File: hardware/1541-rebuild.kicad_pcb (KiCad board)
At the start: 2 copper layers, 76.2 x 97.8 mm, 30 parts, among them CON1 SD_Card, IC1 ATMEGA1284P-P, J1 ISP, J2 KEYS, J3 EXT_5V, J4 RESET CONN, J5 PC7, J6 LCD Display, P1 VIA_PIN_1-20, P2 VIA-6522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

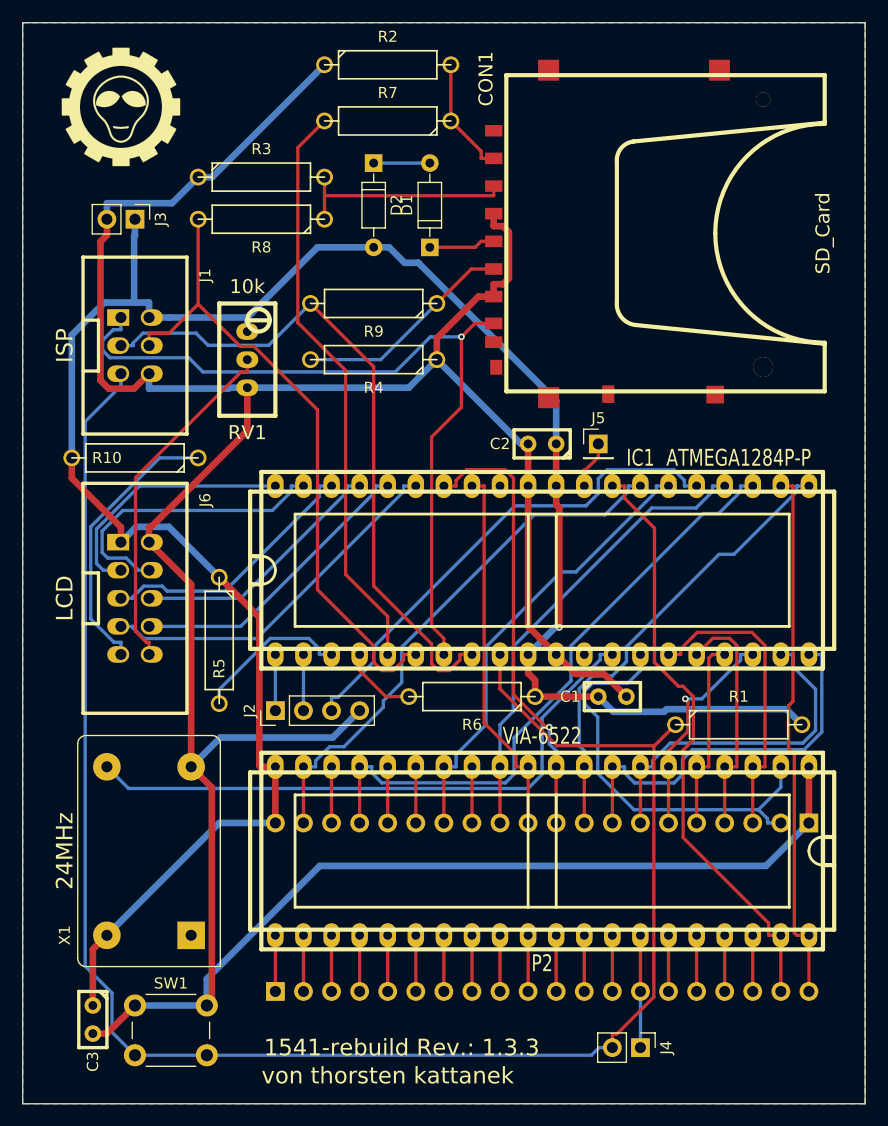
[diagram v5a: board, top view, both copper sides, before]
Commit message: - Hardware nochmal angepasst - erstes Layout erstellt - Schaltplan auf Rev.1.3.4 gesetzt
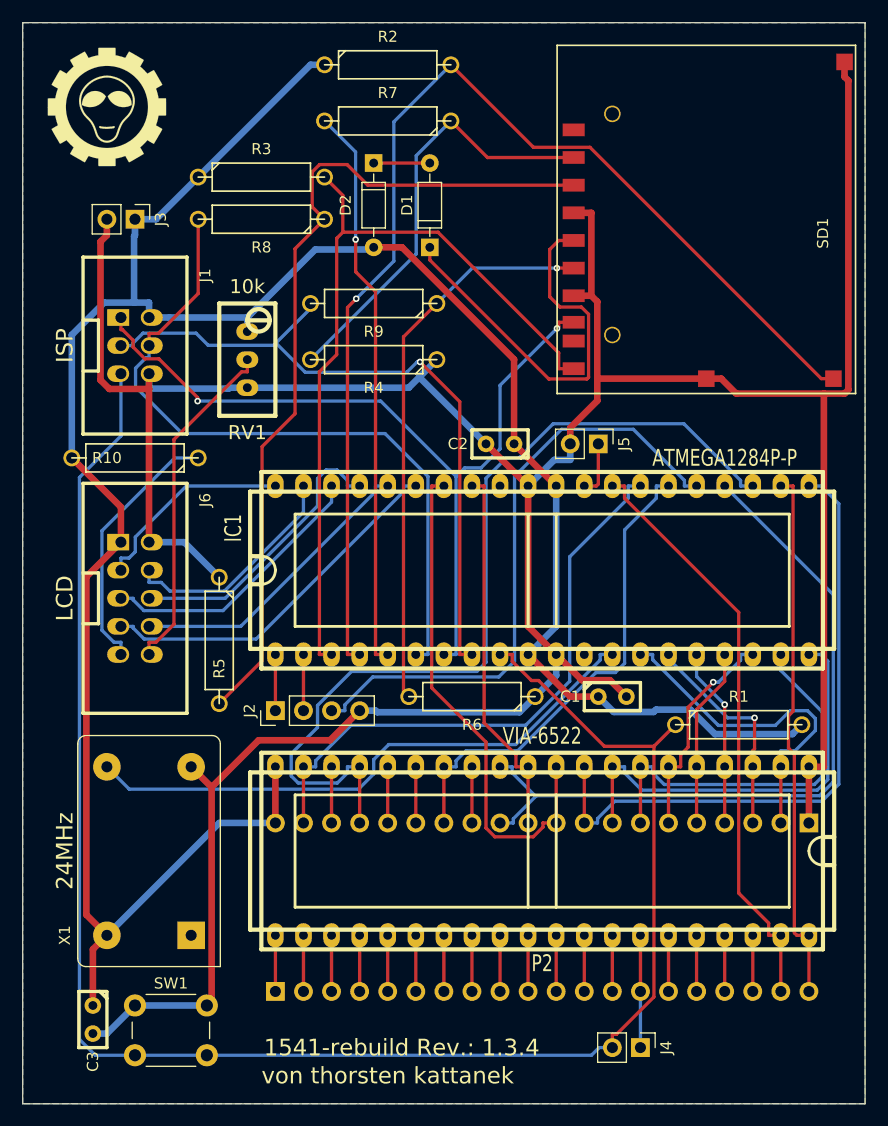
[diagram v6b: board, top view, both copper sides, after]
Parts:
- removed CON1: SD_Card, w_conn_misc:sd_socket
- removed the G*** at (116.8, 49.5)
- added G***: LOGO, ka_logos:logo_01_10_7mm_fsilk, F.Cu at (115.6, 49.5)
- added SD1: SD_Socket, ka_sd_sockets:SD_Socket_104D-TCA0-R06, F.Cu at (161.3, 61.0)
- J5: footprint Pin_Headers:Pin_Header_Straight_1x01_Pitch2.54mm -> Pin_Headers:Pin_Header_Straight_1x02_Pitch2.54mm
- R2: value 3,3k -> 47k
- R3: value 3,3k -> 47kR
- R5: value 47k -> 3,3k
- R6: value 47kR -> 3,3k
- moved C2 3.81 mm to (151.1, 80.0)
- turned J5 to 270 degrees
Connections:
- R2 pad 1: GND -> +5V
- R2 pad 2: Net-(CON1-Pad1) -> /SD Karte/SD_WP
- R3 pad 1: GND -> +5V
- R3 pad 2: Net-(CON1-Pad2) -> /SD Karte/SD_DETECT
- R4 pad 2: Net-(CON1-Pad5) -> Net-(R4-Pad2)
- R5 pad 1: +5V -> GND
- R5 pad 2: /SD Karte/SD_DETECT -> Net-(R5-Pad2)
- R6 pad 1: +5V -> GND
- R6 pad 2: /SD Karte/SD_WP -> Net-(R6-Pad2)
- R7 pad 1: Net-(CON1-Pad1) -> Net-(R4-Pad2)
- R8 pad 1: Net-(CON1-Pad2) -> Net-(R5-Pad2)
- R9 pad 1: Net-(CON1-Pad5) -> Net-(R6-Pad2)
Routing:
- net /SD Karte/SD_WP: track 6.87 -> 104.7 mm, vias 0 -> 1
- net Net-(R5-Pad2): track 0.00 -> 77.2 mm
- net /SD Karte/SD_DETECT: track 14.2 -> 72.7 mm
- net Net-(R6-Pad2): track 0.00 -> 50.7 mm, vias 0 -> 1
- net Net-(R4-Pad2): track 0.00 -> 39.3 mm
- net Net-(D1-Pad1): track 6.00 -> 36.7 mm
- net +5V: track 200.9 -> 228.4 mm, vias 1 -> 0
- net /VIA 6522 Sockel/MTR: track 41.9 -> 67.4 mm
- net /VIA 6522 Sockel/SYNC: track 56.8 -> 82.1 mm
- net Net-(CON1-Pad2): track 20.0 -> 0.00 mm
- net Net-(CON1-Pad5): track 20.0 -> 0.00 mm
- net /VIA 6522 Sockel/PA7: track 41.8 -> 58.5 mm
- net GND: track 291.3 -> 305.3 mm
- net Net-(IC1-Pad25): track 45.2 -> 56.1 mm
- net Net-(CON1-Pad1): track 10.7 -> 0.00 mm
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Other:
- board text added: "1541-rebuild Rev.: 1.3.4"
- board text removed: "1541-rebuild Rev.: 1.3.3"

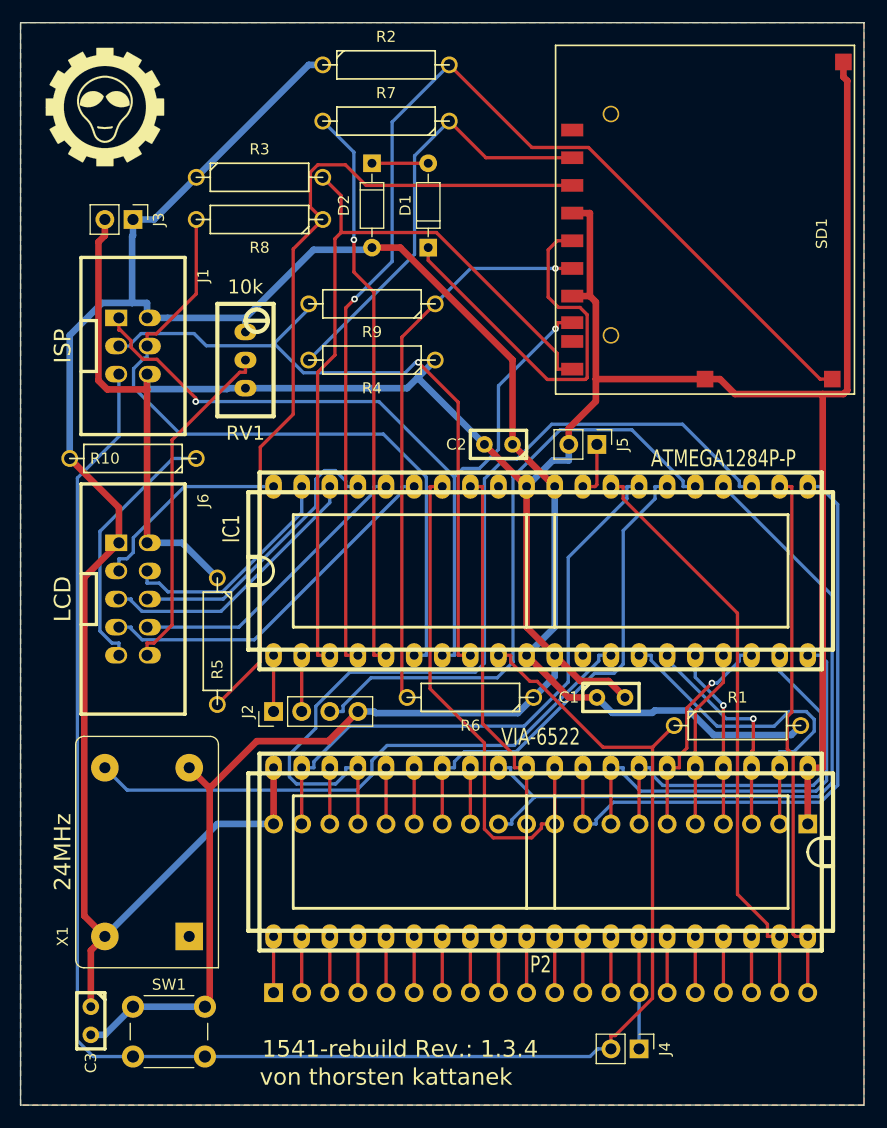
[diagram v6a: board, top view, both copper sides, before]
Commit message: Borad fertig gestellt und auf rev 1.3.5 gesetzt Gerberfiles erzeugt und als rar gepackt. Mit PCB Hersteller -Seedstudio- getestet.
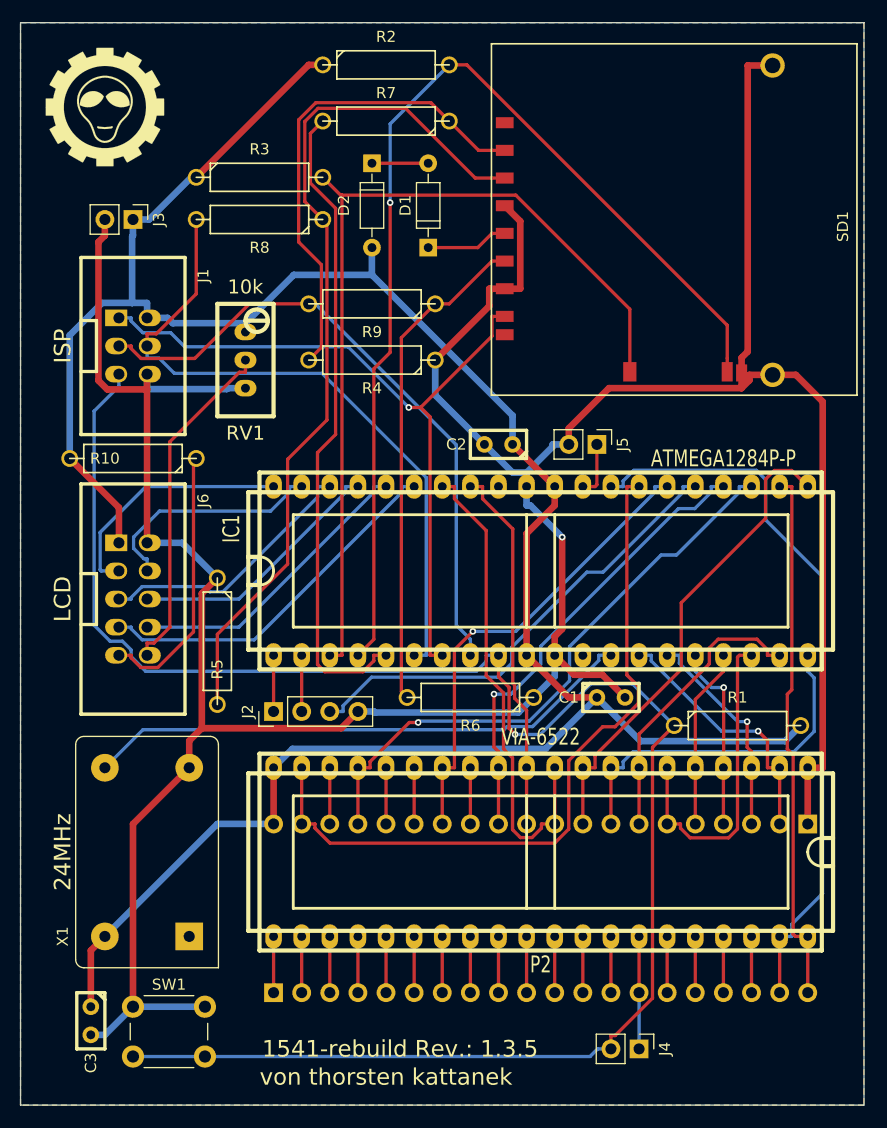
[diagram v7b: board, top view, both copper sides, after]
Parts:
- SD1: value SD_Socket -> ATTEND_104H-TDA0-R01; footprint ka_sd_sockets:SD_Socket_104D-TCA0-R06 -> ka_sd_sockets:ATTEND_104H-TDA0-R01
- moved SD1 14.6 mm to (175.9, 60.3)
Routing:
- net Net-(D1-Pad1): track 36.7 -> 7.45 mm
- net /VIA 6522 Sockel/SYNC: track 82.1 -> 53.6 mm, vias 0 -> 1
- net /VIA 6522 Sockel/MTR: track 67.4 -> 41.6 mm, vias 0 -> 1
- net /VIA 6522 Sockel/PA7: track 58.5 -> 43.4 mm
- net Net-(IC1-Pad25): track 56.1 -> 42.9 mm
- net /VIA 6522 Sockel/OE: track 53.6 -> 66.4 mm
- net /VIA 6522 Sockel/SOE: track 53.3 -> 66.0 mm
- net /VIA 6522 Sockel/PA4: track 20.0 -> 29.4 mm, vias 1 -> 0
- net /VIA 6522 Sockel/PA5: track 35.4 -> 26.1 mm
- net /SD Karte/SD_WP: track 104.7 -> 95.8 mm
- net /SD Karte/SD_DETECT: track 72.7 -> 81.0 mm
- net +5V: track 228.4 -> 220.3 mm
- net /SD Karte/MISO: track 74.7 -> 66.7 mm, vias 2 -> 1
- net /VIA 6522 Sockel/PA0: track 31.1 -> 23.7 mm, vias 0 -> 1
- net /SD Karte/SS: track 51.3 -> 58.5 mm, vias 1 -> 0
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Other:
- board text added: "1541-rebuild Rev.: 1.3.5"
- board text removed: "1541-rebuild Rev.: 1.3.4"

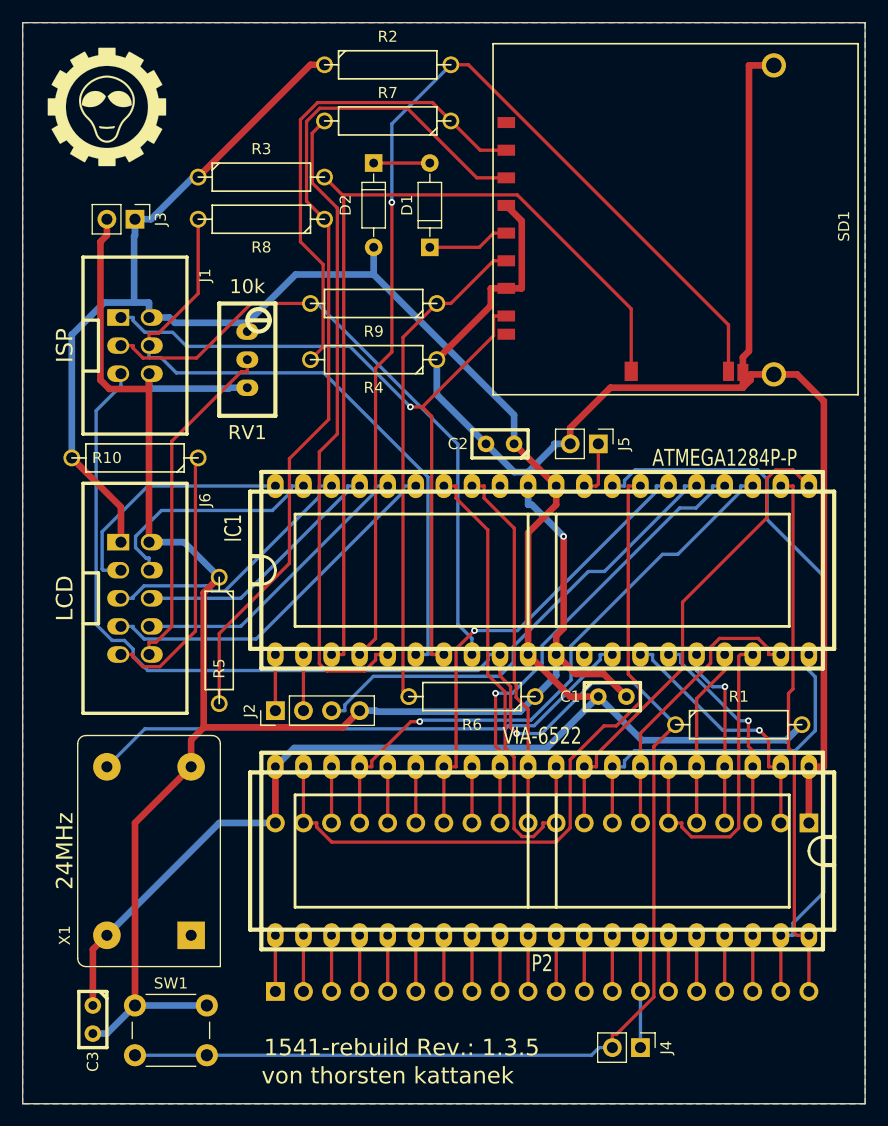
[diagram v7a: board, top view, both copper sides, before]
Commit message: Hardware Projekt knovertiert von KiCad 4 -> KiCad 5 - Schaltplan angepasst - neues Detailfoto hinzugefügt - Footprints neu zugeordnet, somit ist auch wieder eine 3D Darstellung möglich - Readme.md angepasst
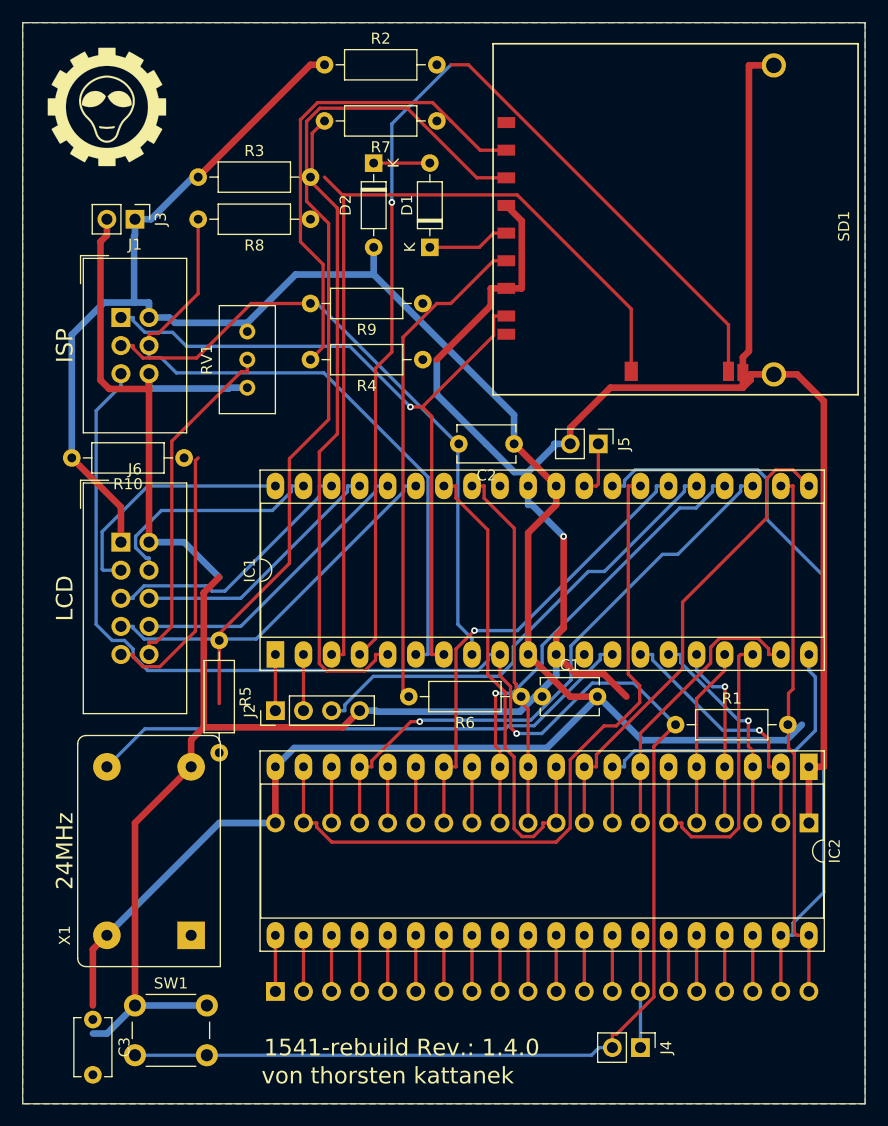
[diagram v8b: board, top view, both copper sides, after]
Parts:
- removed the G*** at (115.6, 49.5)
- removed P3: VIA_PIN_21-40, Pin_Headers:Pin_Header_Straight_1x20_Pitch2.54mm
- added G***: LOGO, logos_tk:logo_01_10_7mm_fsilk, F.Cu at (115.6, 49.5)
- added IC2: VIA6522, Package_DIP:DIP-40_W15.24mm_Socket_LongPads, F.Cu at (179.1, 109.2)
- C1, C2, C3: footprint w_capacitors:cnp_3mm_disc -> Capacitor_THT:C_Disc_D5.1mm_W3.2mm_P5.00mm
- D1, D2: footprint Diodes_THT:D_DO-35_SOD27_P7.62mm_Horizontal -> Diode_THT:D_DO-35_SOD27_P7.62mm_Horizontal
- IC1: footprint w_pth_circuits:dil_40-600_socket -> Package_DIP:DIP-40_W15.24mm_Socket_LongPads
- J1: footprint w_conn_strip:vasch_strip_3x2 -> Connector_IDC:IDC-Header_2x03_P2.54mm_Vertical
- J2: footprint Pin_Headers:Pin_Header_Straight_1x04_Pitch2.54mm -> Connector_PinHeader_2.54mm:PinHeader_1x04_P2.54mm_Vertical
- J3, J4, J5: footprint Pin_Headers:Pin_Header_Straight_1x02_Pitch2.54mm -> Connector_PinHeader_2.54mm:PinHeader_1x02_P2.54mm_Vertical
- J6: footprint w_conn_strip:vasch_strip_5x2 -> Connector_IDC:IDC-Header_2x05_P2.54mm_Vertical
- P1: footprint Pin_Headers:Pin_Header_Straight_1x20_Pitch2.54mm -> Connector_PinHeader_2.54mm:PinHeader_1x20_P2.54mm_Vertical
- P2: value VIA-6522 -> VIA_PIN_21-40; footprint w_pth_circuits:dil_40-600_socket -> Connector_PinHeader_2.54mm:PinHeader_1x20_P2.54mm_Vertical; moved to B.Cu
- R1, R10, R2, R4, R5, R6, R7, R8, R9: footprint Discret:R4-5 -> Resistor_THT:R_Axial_DIN0207_L6.3mm_D2.5mm_P10.16mm_Horizontal
- R3: value 47kR -> 47k; footprint Discret:R4-5 -> Resistor_THT:R_Axial_DIN0207_L6.3mm_D2.5mm_P10.16mm_Horizontal
- RV1: footprint w_pth_resistors:trimmer_vishay_64w -> Potentiometer_THT:Potentiometer_Bourns_3296W_Vertical
- SD1: footprint ka_sd_sockets:ATTEND_104H-TDA0-R01 -> sd_sockets_tk:ATTEND_104H-TDA0-R01
- SW1: footprint Buttons_Switches_THT:SW_PUSH_6mm_h5mm -> Button_Switch_THT:SW_PUSH_6mm_H5mm
- X1: footprint Oscillators:Oscillator_DIP-14_LargePads -> Oscillator:Oscillator_DIP-14_LargePads
- moved P2 27.3 mm to (130.8, 129.5), turned to 270 degrees
- moved IC1 25.3 mm to (130.8, 99.1), turned to 90 degrees
- moved C1 6.35 mm to (154.9, 102.9)
- moved R1 5.72 mm to (167.0, 105.4)
- moved R2 5.72 mm to (135.3, 45.7)
- moved R3 5.71 mm to (123.8, 55.9)
- moved J6 5.24 mm to (116.8, 88.9), turned to 0 degrees
- moved R4 4.45 mm to (144.1, 72.4)
- moved R8 4.45 mm to (134.0, 59.7)
- moved R9 4.45 mm to (144.1, 67.3)
- moved R10 4.45 mm to (122.6, 81.3)
- moved R6 4.44 mm to (153.0, 102.9)
- moved R7 4.44 mm to (145.4, 50.8)
- moved J1 2.84 mm to (116.8, 68.6), turned to 0 degrees
- moved RV1 2.54 mm to (128.3, 69.8), turned to 90 degrees
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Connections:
- net /LCD Display/D0 renamed /LCD Display/D4
- net /LCD Display/D1 renamed /LCD Display/D5
- net /LCD Display/D2 renamed /LCD Display/D6
- net /LCD Display/D3 renamed /LCD Display/D7
- P2 pad 1: GND -> Net-(IC2-Pad21)
- P2 pad 10: /VIA 6522 Sockel/STP1 -> Net-(IC2-Pad30)
- P2 pad 11: /VIA 6522 Sockel/SPT0 -> Net-(IC2-Pad31)
- P2 pad 12: /VIA 6522 Sockel/MTR -> Net-(IC2-Pad32)
- P2 pad 13: /VIA 6522 Sockel/ACT -> Net-(IC2-Pad33)
- P2 pad 14: /VIA 6522 Sockel/WPS -> /VIA 6522 Sockel/~RESET
- P2 pad 15: /VIA 6522 Sockel/DS0 -> Net-(IC2-Pad35)
- P2 pad 16: /VIA 6522 Sockel/DS1 -> Net-(IC2-Pad36)
- P2 pad 17: /VIA 6522 Sockel/SYNC -> Net-(IC2-Pad37)
- P2 pad 18: /VIA 6522 Sockel/NC -> Net-(IC2-Pad38)
- P2 pad 19: /VIA 6522 Sockel/OE -> /VIA 6522 Sockel/SOE
- P2 pad 2: /VIA 6522 Sockel/PA0 -> Net-(IC2-Pad22)
- P2 pad 20: +5V -> /VIA 6522 Sockel/BRDY
- P2 pad 3: /VIA 6522 Sockel/PA1 -> Net-(IC2-Pad23)
- P2 pad 4: /VIA 6522 Sockel/PA2 -> Net-(IC2-Pad24)
- P2 pad 5: /VIA 6522 Sockel/PA3 -> Net-(IC2-Pad25)
- P2 pad 6: /VIA 6522 Sockel/PA4 -> Net-(IC2-Pad26)
- P2 pad 7: /VIA 6522 Sockel/PA5 -> Net-(IC2-Pad27)
- P2 pad 8: /VIA 6522 Sockel/PA6 -> Net-(IC2-Pad28)
- P2 pad 9: /VIA 6522 Sockel/PA7 -> Net-(IC2-Pad29)
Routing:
- net GND: track 305.5 -> 417.5 mm
- net Net-(R5-Pad2): track 78.8 -> 0.00 mm
- net /LCD Display/EN: track 33.3 -> 0.00 mm
- net Net-(P2-Pad38): track 5.08 -> 0.00 mm
- net Net-(P2-Pad37): track 5.08 -> 0.00 mm
- net Net-(P2-Pad36): track 5.08 -> 0.00 mm
- net Net-(P2-Pad35): track 5.08 -> 0.00 mm
- net Net-(P2-Pad33): track 5.08 -> 0.00 mm
- net Net-(P2-Pad32): track 5.08 -> 0.00 mm
- net Net-(P2-Pad31): track 5.08 -> 0.00 mm
- net Net-(P2-Pad30): track 5.08 -> 0.00 mm
- net Net-(P2-Pad29): track 5.08 -> 0.00 mm
- net Net-(P2-Pad28): track 5.08 -> 0.00 mm
- net Net-(P2-Pad27): track 5.08 -> 0.00 mm
- net Net-(P2-Pad26): track 5.08 -> 0.00 mm
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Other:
- board text added: "1541-rebuild Rev.: 1.4.0"
- board text removed: "1541-rebuild Rev.: 1.3.5"
